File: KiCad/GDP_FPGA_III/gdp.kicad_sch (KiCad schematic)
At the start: 14 parts, among them J1 NKC-Bus, U2 74HC245, U3 74HC245, U4 74HC245

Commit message: update
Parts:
- U2, U3, U4: value 74HC245 -> 74LVC245
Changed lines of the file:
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@@
       (effects (font (size 1.27 1.27)) (justify left))
     )
-    (property "Value" "74HC245" (at 221.9041 56.515 0)
+    (property "Value" "74LVC245" (at 221.9041 56.515 0)
       (effects (font (size 1.27 1.27)) (justify left))
     )
@@
       (effects (font (size 1.27 1.27)) (justify left))
     )
-    (property "Value" "74HC245" (at 223.1741 109.855 0)
+    (property "Value" "74LVC245" (at 223.1741 109.855 0)
       (effects (font (size 1.27 1.27)) (justify left))
     )
@@
       (effects (font (size 1.27 1.27)) (justify left))
     )
-    (property "Value" "74HC245" (at 223.1741 165.1 0)
-      (effects (font (size 1.27 1.27)) (justify left))
-    )
+    (property "Value" "74LVC245" (at 223.1741 165.1 0)
+      (effects (font (size 1.27 1.27)) (justify left))
+    )

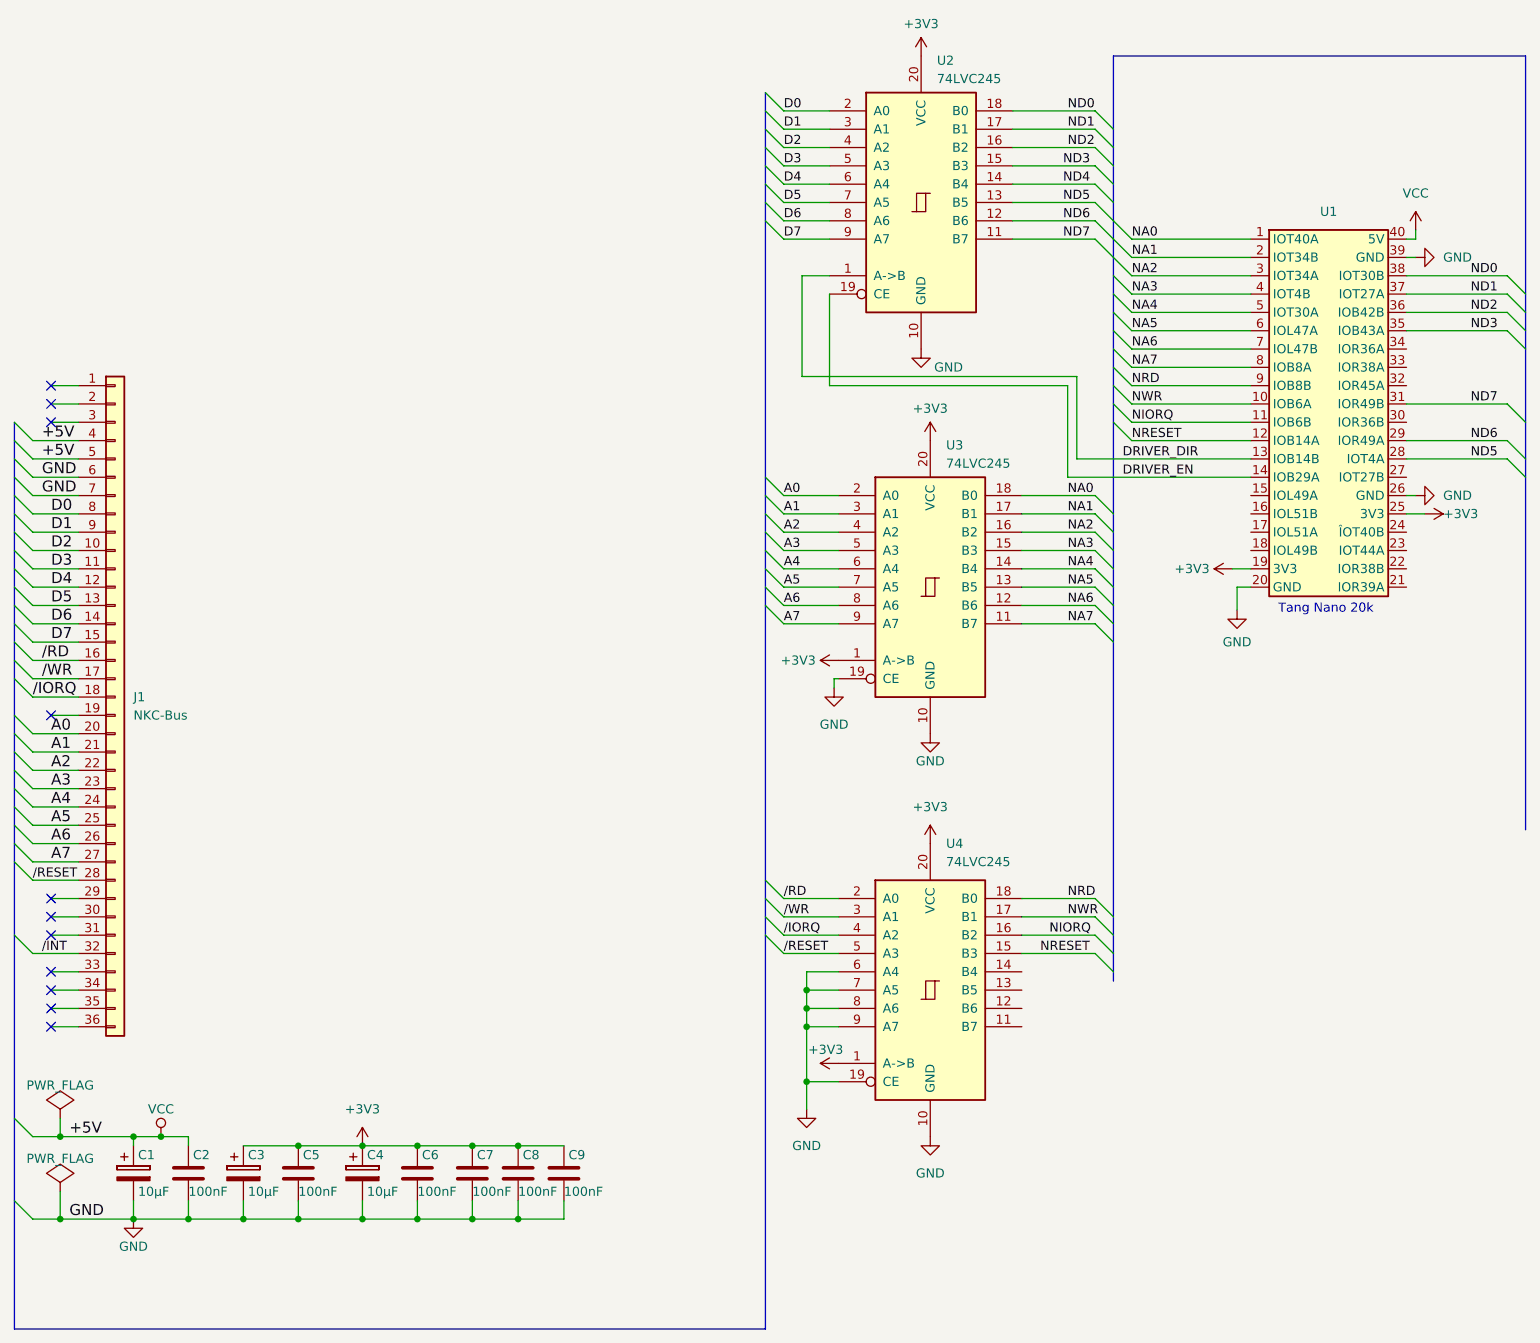
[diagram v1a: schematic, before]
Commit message: remap some pins to enable SDCARD usage
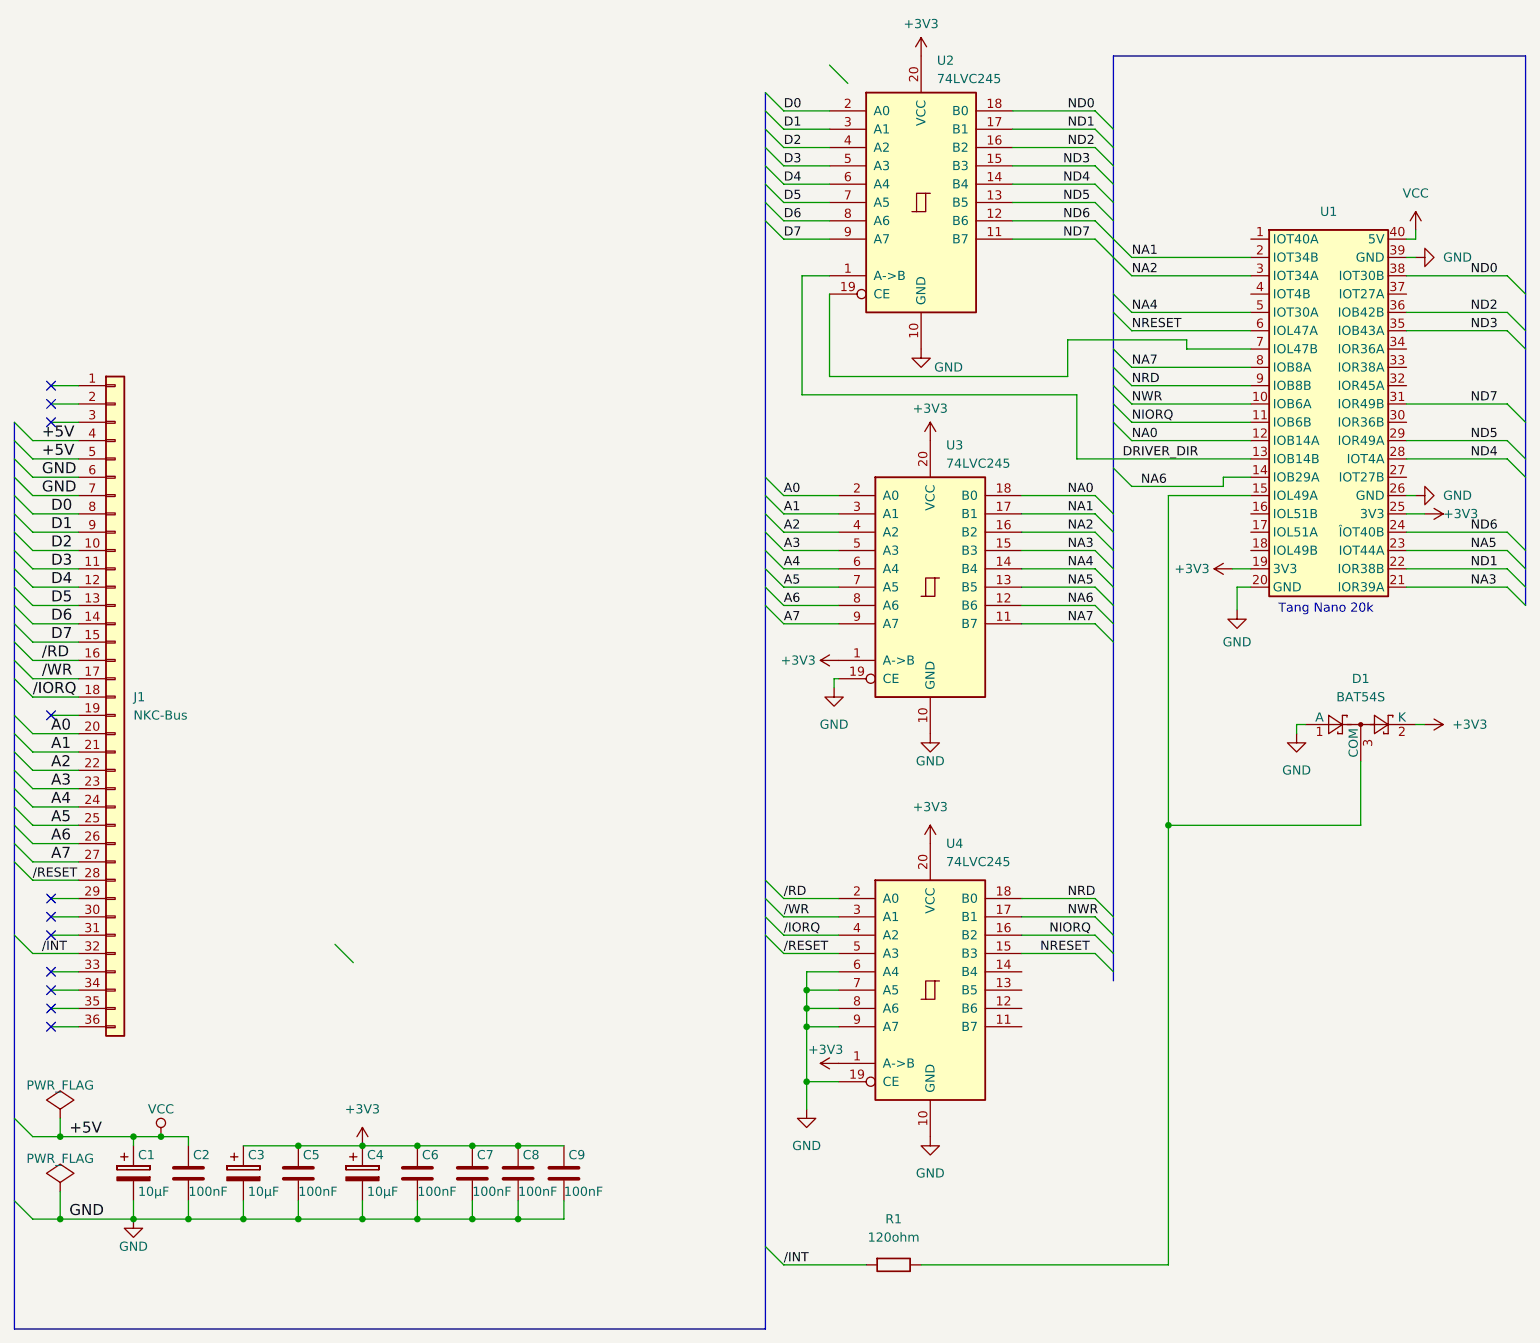
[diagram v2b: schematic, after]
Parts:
- added D1: BAT54S, Package_TO_SOT_SMD:SOT-23, symbol Diode:BAT54S
- added R1: 120ohm, Resistor_THT:R_Axial_DIN0207_L6.3mm_D2.5mm_P10.16mm_Horizontal, symbol PCM_SL_Resistors:120ohm
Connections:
- net +3V3: now also D1.2 (K)
- net GND: now also D1.1 (A)
- net NA0: now also U1.12 (IOB14A); no longer U1.1 (IOT40A)
- net NA3: now also U1.21 (IOR39A); no longer U1.4 (IOT4B)
- net NA5: now also U1.23 (IOT44A); no longer U1.6 (IOL47A)
- net NA6: now also U1.14 (IOB29A); no longer U1.7 (IOL47B)
- net ND1: now also U1.22 (IOR38B); no longer U1.37 (IOT27A)
- net ND4: now also U1.28 (IOT4A)
- net ND5: now also U1.29 (IOR49A); no longer U1.28 (IOT4A)
- net ND6: now also U1.24 (ÎOT40B); no longer U1.29 (IOR49A)
- net NRESET: now also U1.6 (IOL47A); no longer U1.12 (IOB14A)
- net /INT: now also R1.1
- net at U1.15 (IOL49A): now also D1.3 (COM), R1.2
- net DRIVER_EN: no longer names the net of U2.19 (CE)
- net DRIVER_EN: now also U1.7 (IOL47B); no longer U1.14 (IOB29A)
